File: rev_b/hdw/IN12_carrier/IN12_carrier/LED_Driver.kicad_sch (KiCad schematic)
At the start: 20 parts, among them U2101 LP5009

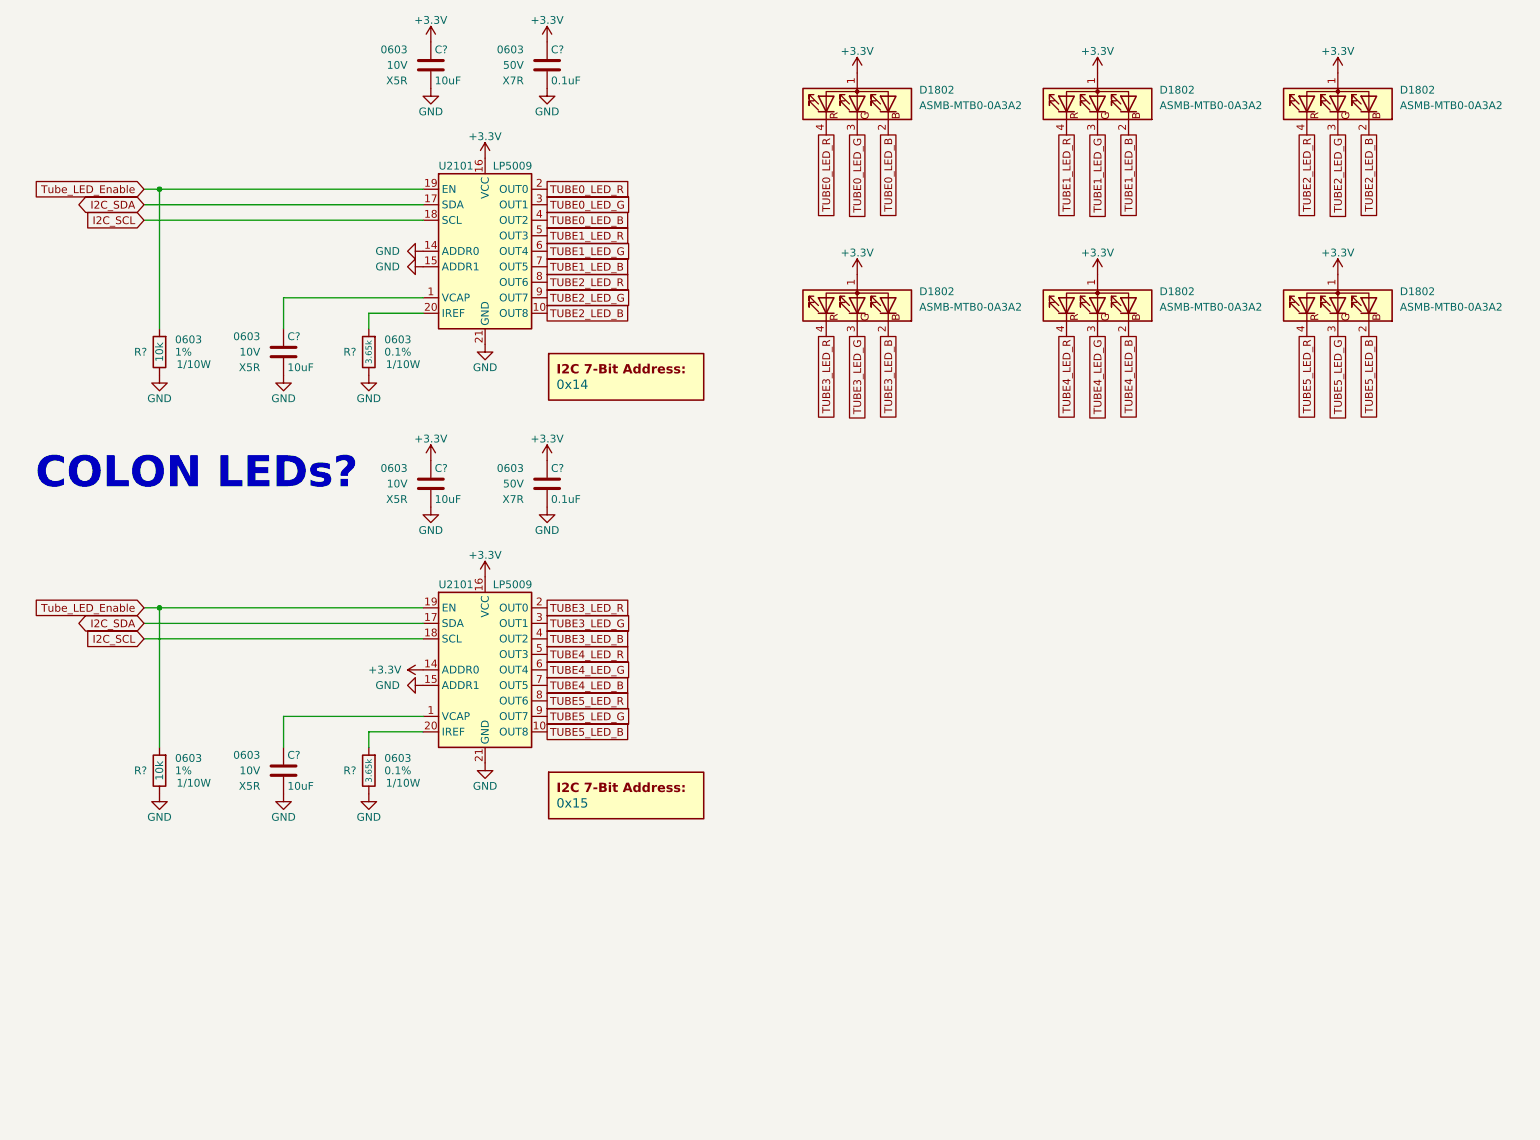
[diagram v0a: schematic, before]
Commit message: updated footprints, ran some DRC
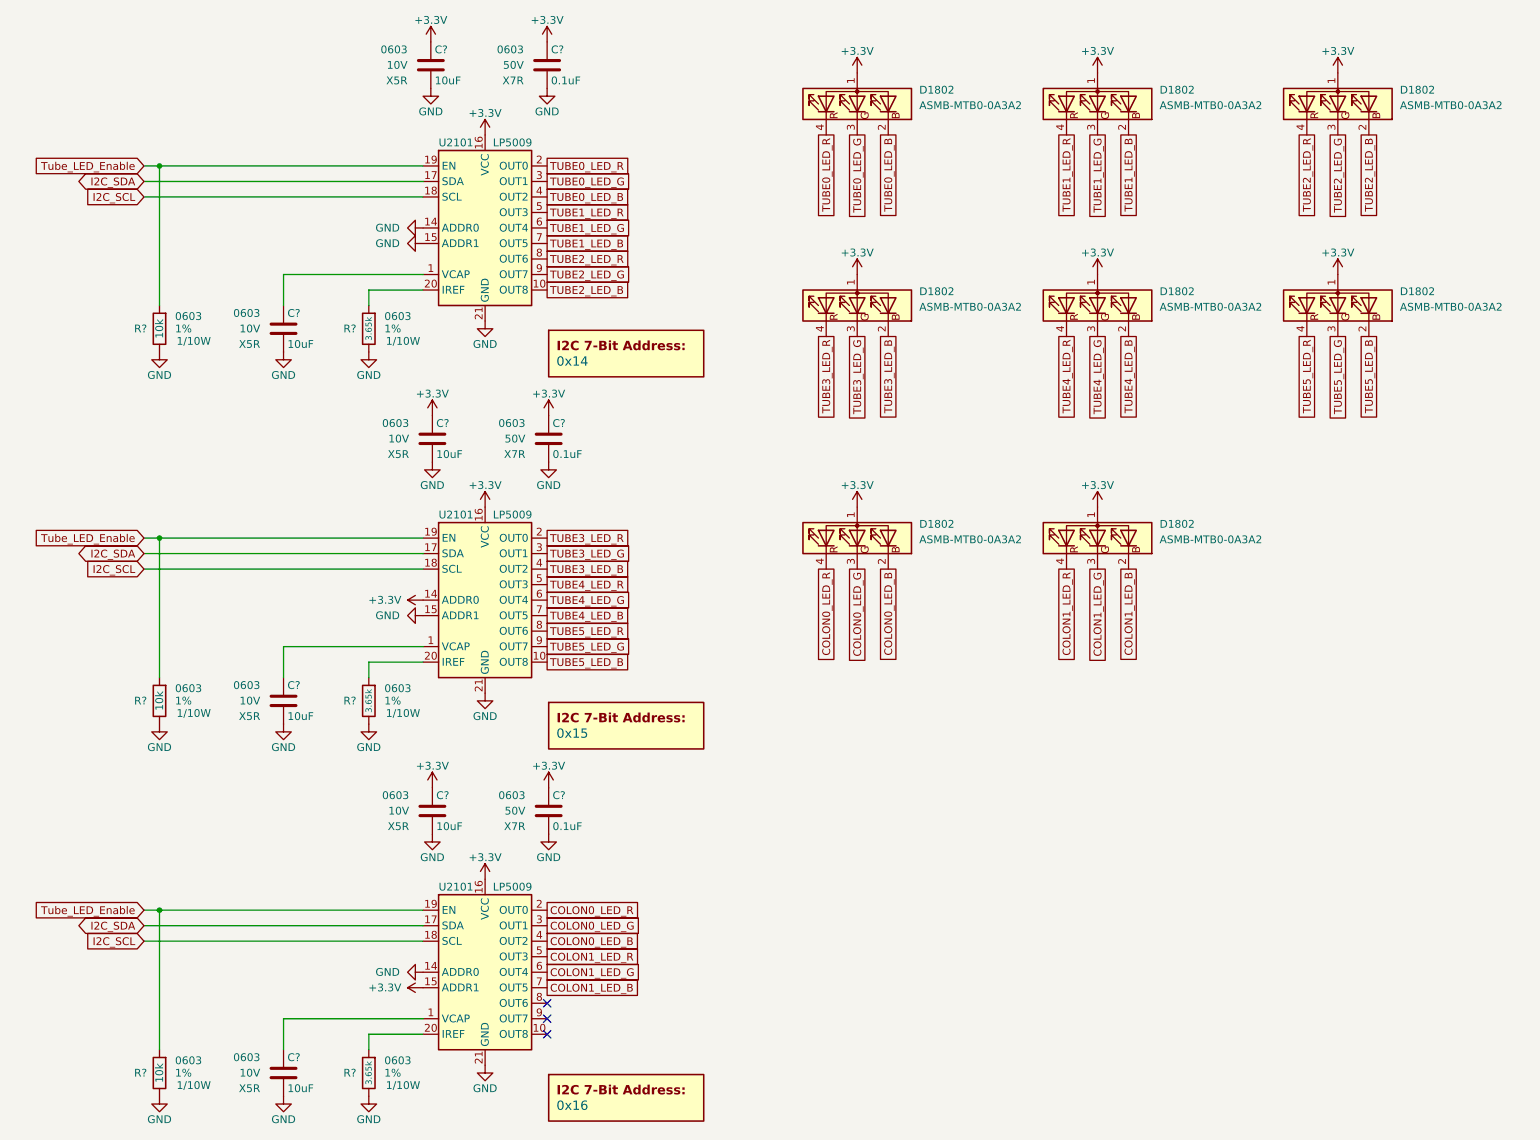
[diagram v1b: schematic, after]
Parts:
- added C?: 0.1uF, Capacitors_SMD:C_0603, symbol Custom_Library:C_Custom
- added C? (x2): 10uF, Capacitors_SMD:C_0603, symbol Custom_Library:C_Custom
- added D1802 (x2): ASMB-MTB0-0A3A2, LED_SMD:LED_Avago_PLCC4_3.2x2.8mm_CW, symbol LED:ASMB-MTB0-0A3A2
- added DOC2101: 0x16, symbol Custom_Library:I2C_Address
- added R?: 10k, Resistors_SMD:R_0603, symbol Custom_Library:R_Custom
- added R?: 3.65k, Resistors_SMD:R_0603, symbol Custom_Library:R_Custom
- added U2101: LP5009, Housings_DFN_QFN:UQFN-20-1EP_3x3mm_Pitch0.4mm, symbol Custom_Library:LP5009
- C? (x2): Digi-Key PN 399-7845-1-ND -> (none)
- C? (x4): Digi-Key PN 490-10474-1-ND -> (none)
- R? (x2): Digi-Key PN YAG2321CT-ND -> (none)
- R? (x2): Digi-Key PN YAG4547CT-ND -> (none); Tolerance 0.1% -> 1%
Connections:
- net +3V3: now also C?.1, C?.1, D1802.1 (A), D1802.1 (A), U2101.15 (ADDR1), U2101.16 (VCC)
- net GND: now also C?.2, C?.2, C?.2, R?.2, R?.2, U2101.14 (ADDR0), U2101.21 (GND)
- net I2C_SCL: now also U2101.18 (SCL)
- net I2C_SDA: now also U2101.17 (SDA)
- net Tube_LED_Enable: now also R?.1, U2101.19 (EN)
- new net: R?.1, U2101.20 (IREF)
- new net: C?.1, U2101.1 (VCAP)
- new net COLON0_LED_B: D1802.2 (BK), U2101.4 (OUT2)
- new net COLON0_LED_G: D1802.3 (GK), U2101.3 (OUT1)
- new net COLON0_LED_R: D1802.4 (RK), U2101.2 (OUT0)
- new net COLON1_LED_B: D1802.2 (BK), U2101.7 (OUT5)
- new net COLON1_LED_G: D1802.3 (GK), U2101.6 (OUT4)
- new net COLON1_LED_R: D1802.4 (RK), U2101.5 (OUT3)
- no-connect marks 0 -> 3
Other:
- note removed: "COLON LEDs?"
- moved on the sheet: C?, R?, U2101

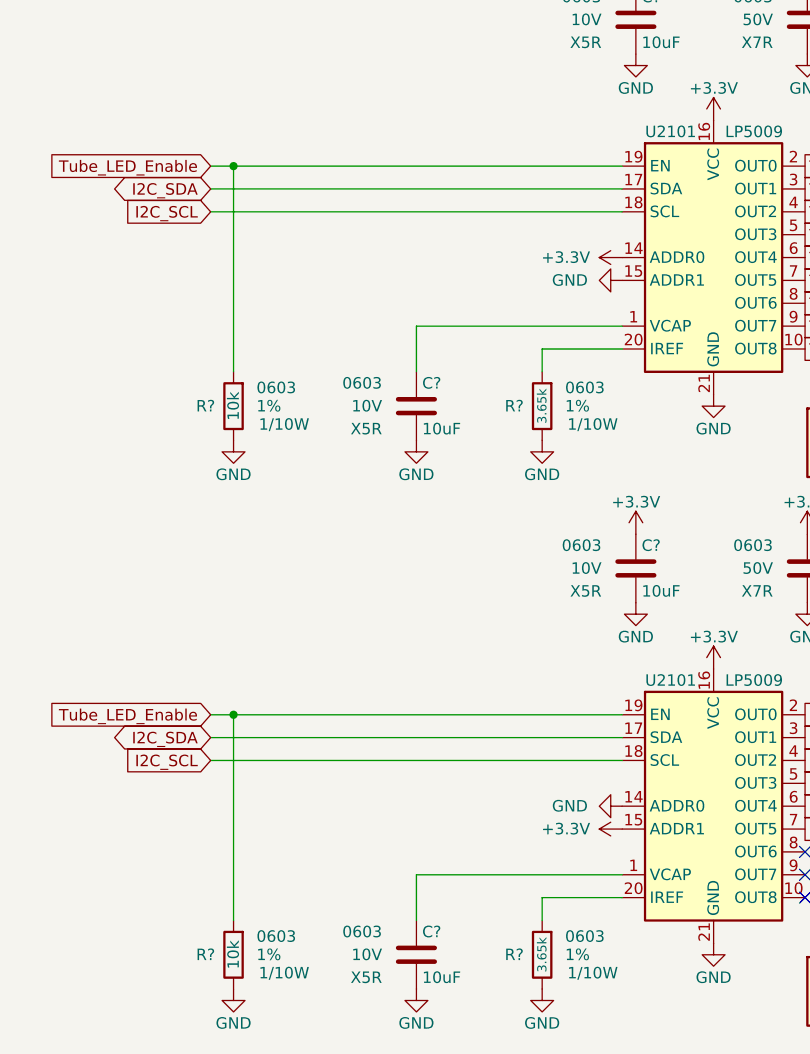
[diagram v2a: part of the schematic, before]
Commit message: lots of placement progress on IN12 carrier board
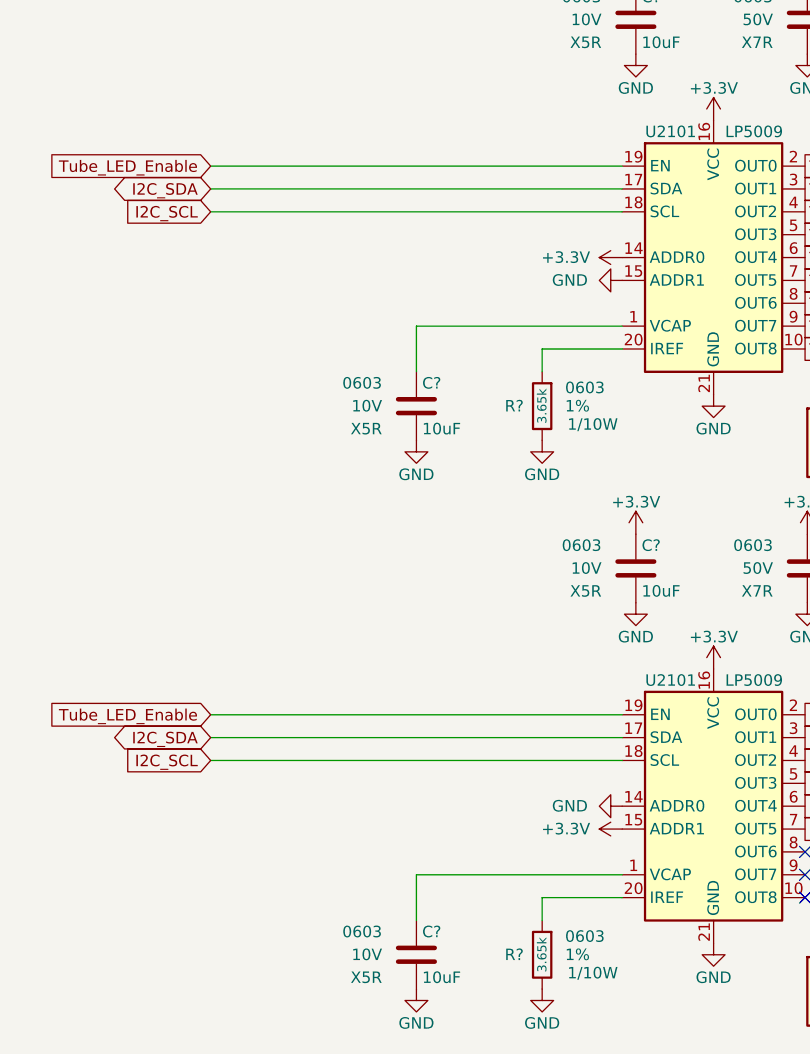
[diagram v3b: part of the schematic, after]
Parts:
- removed R? (x2): 10k, Resistors_SMD:R_0603, symbol Custom_Library:R_Custom
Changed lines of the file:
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@@
     (company "Drew Maatman")
-  )
-  (junction (at 40.64 105.41) (diameter 0) (color 0 0 0 0)
-  )
-  (junction (at 40.64 166.37) (diameter 0) (color 0 0 0 0)
   )
   (junction (at 40.64 44.45) (diameter 0) (color 0 0 0 0)
@@
     (stroke (width 0) (type default))
   )
-  (wire (pts (xy 40.64 105.41) (xy 83.82 105.41))
+  (wire (pts (xy 38.1 105.41) (xy 83.82 105.41))
     (stroke (width 0) (type default))
   )
-  (wire (pts (xy 40.64 166.37) (xy 83.82 166.37))
+  (wire (pts (xy 38.1 166.37) (xy 83.82 166.37))
     (stroke (width 0) (type default))
   )
@@
     (stroke (width 0) (type default))
   )
-  (wire (pts (xy 40.64 189.23) (xy 40.64 166.37))
-    (stroke (width 0) (type default))
-  )
   (wire (pts (xy 60.96 62.23) (xy 60.96 67.31))
     (stroke (width 0) (type default))
@@
     (stroke (width 0) (type default))
   )
-  (wire (pts (xy 38.1 166.37) (xy 40.64 166.37))
-    (stroke (width 0) (type default))
-  )
   (wire (pts (xy 83.82 123.19) (xy 60.96 123.19))
     (stroke (width 0) (type default))
   )
   (wire (pts (xy 38.1 171.45) (xy 83.82 171.45))
-    (stroke (width 0) (type default))
-  )
-  (wire (pts (xy 38.1 105.41) (xy 40.64 105.41))
-    (stroke (width 0) (type default))
-  )
-  (wire (pts (xy 40.64 128.27) (xy 40.64 105.41))
     (stroke (width 0) (type default))
   )
@@
     )
   )
-  (symbol (lib_id "Custom_Library:R_Custom") (at 40.64 193.04 0) (unit 1)
-    (in_bom yes) (on_board yes) (dnp no)
-    (property "Reference" "R?" (at 38.608 193.04 0)
-      (effects (font (size 1.27 1.27)) (justify right))
-    )
-    (property "Value" "10k" (at 40.64 193.04 90)
-      (effects (font (size 1.27 1.27)))
-    )
-    (property "Footprint" "Resistors_SMD:R_0603" (at 40.64 193.04 0)
-      (effects (font (size 1.27 1.27)) hide)
-    )
-    (property "Datasheet" "" (at 40.64 193.04 0)
-      (effects (font (size 1.27 1.27)) hide)
-    )
-    (property "display_footprint" "0603" (at 43.18 191.008 0)
-      (effects (font (size 1.27 1.27)) (justify left))
-    )
-    (property "Tolerance" "1%" (at 43.18 193.04 0)
-      (effects (font (size 1.27 1.27)) (justify left))
-    )
-    (property "Wattage" "1/10W" (at 43.434 195.072 0)
-      (effects (font (size 1.27 1.27)) (justify left))
-    )
-    (property "Digi-Key PN" "" (at 48.26 182.88 0)
-      (effects (font (size 1.524 1.524)) hide)
-    )
-    (pin "1")
-    (pin "2")
-    (instances
-      (project "Analog_Clock"
-        (path "/b40d07ca-3b69-4fcb-b15e-f8aade07e509/00000000-0000-0000-0000-00005bb27bf7"
-          (reference "R?") (unit 1)
-        )
-        (path "/b40d07ca-3b69-4fcb-b15e-f8aade07e509/00000000-0000-0000-0000-00005c1e3a08"
-          (reference "R?") (unit 1)
-        )
-        (path "/b40d07ca-3b69-4fcb-b15e-f8aade07e509/00000000-0000-0000-0000-00005cb7718d"
-          (reference "R?") (unit 1)
-        )
-        (path "/b40d07ca-3b69-4fcb-b15e-f8aade07e509/00000000-0000-0000-0000-00005e0f263a"
-          (reference "R?") (unit 1)
-        )
-        (path "/b40d07ca-3b69-4fcb-b15e-f8aade07e509/00000000-0000-0000-0000-00005e98cf45"
-          (reference "R?") (unit 1)
-        )
-        (path "/b40d07ca-3b69-4fcb-b15e-f8aade07e509/00000000-0000-0000-0000-00005bb27ba3"
-          (reference "R?") (unit 1)
-        )
-        (path "/b40d07ca-3b69-4fcb-b15e-f8aade07e509/00000000-0000-0000-0000-00005d779ae1"
-          (reference "R?") (unit 1)
-        )
-        (path "/b40d07ca-3b69-4fcb-b15e-f8aade07e509/00000000-0000-0000-0000-00005e939d31"
-          (reference "R?") (unit 1)
-        )
-        (path "/b40d07ca-3b69-4fcb-b15e-f8aade07e509/00000000-0000-0000-0000-00005c1de17a"
-          (reference "R?") (unit 1)
-        )
-        (path "/b40d07ca-3b69-4fcb-b15e-f8aade07e509/00000000-0000-0000-0000-00005f280e04"
-          (reference "R2101") (unit 1)
-        )
-        (path "/b40d07ca-3b69-4fcb-b15e-f8aade07e509/00000000-0000-0000-0000-00005e0dc082"
-          (reference "R?") (unit 1)
-        )
-      )
-      (project "IN12_carrier"
-        (path "/c4d83a5b-e6ae-4326-9df5-0c4ac01f7d8c/c710c274-9ef6-4493-9995-cccebf092ebf"
-          (reference "R703") (unit 1)
-        )
-      )
-    )
-  )
   (symbol (lib_id "Analog_Clock-rescue:+3.3V-power") (at 85.344 146.304 0) (unit 1)
     (in_bom yes) (on_board yes) (dnp no)
@@
         (path "/c4d83a5b-e6ae-4326-9df5-0c4ac01f7d8c/c710c274-9ef6-4493-9995-cccebf092ebf"
           (reference "#PWR0734") (unit 1)
-        )
-      )
-    )
-  )
-  (symbol (lib_id "Custom_Library:R_Custom") (at 40.64 132.08 0) (unit 1)
-    (in_bom yes) (on_board yes) (dnp no)
-    (property "Reference" "R?" (at 38.608 132.08 0)
-      (effects (font (size 1.27 1.27)) (justify right))
-    )
-    (property "Value" "10k" (at 40.64 132.08 90)
-      (effects (font (size 1.27 1.27)))
-    )
-    (property "Footprint" "Resistors_SMD:R_0603" (at 40.64 132.08 0)
-      (effects (font (size 1.27 1.27)) hide)
-    )
-    (property "Datasheet" "" (at 40.64 132.08 0)
-      (effects (font (size 1.27 1.27)) hide)
-    )
-    (property "display_footprint" "0603" (at 43.18 130.048 0)
-      (effects (font (size 1.27 1.27)) (justify left))
-    )
-    (property "Tolerance" "1%" (at 43.18 132.08 0)
-      (effects (font (size 1.27 1.27)) (justify left))
-    )
-    (property "Wattage" "1/10W" (at 43.434 134.112 0)
-      (effects (font (size 1.27 1.27)) (justify left))
-    )
-    (property "Digi-Key PN" "" (at 48.26 121.92 0)
-      (effects (font (size 1.524 1.524)) hide)
-    )
-    (pin "1")
-    (pin "2")
-    (instances
-      (project "Analog_Clock"
-        (path "/b40d07ca-3b69-4fcb-b15e-f8aade07e509/00000000-0000-0000-0000-00005bb27bf7"
-          (reference "R?") (unit 1)
-        )
-        (path "/b40d07ca-3b69-4fcb-b15e-f8aade07e509/00000000-0000-0000-0000-00005c1e3a08"
-          (reference "R?") (unit 1)
-        )
-        (path "/b40d07ca-3b69-4fcb-b15e-f8aade07e509/00000000-0000-0000-0000-00005cb7718d"
-          (reference "R?") (unit 1)
-        )
-        (path "/b40d07ca-3b69-4fcb-b15e-f8aade07e509/00000000-0000-0000-0000-00005e0f263a"
-          (reference "R?") (unit 1)
-        )
-        (path "/b40d07ca-3b69-4fcb-b15e-f8aade07e509/00000000-0000-0000-0000-00005e98cf45"
-          (reference "R?") (unit 1)
-        )
-        (path "/b40d07ca-3b69-4fcb-b15e-f8aade07e509/00000000-0000-0000-0000-00005bb27ba3"
-          (reference "R?") (unit 1)
-        )
-        (path "/b40d07ca-3b69-4fcb-b15e-f8aade07e509/00000000-0000-0000-0000-00005d779ae1"
-          (reference "R?") (unit 1)
-        )
-        (path "/b40d07ca-3b69-4fcb-b15e-f8aade07e509/00000000-0000-0000-0000-00005e939d31"
-          (reference "R?") (unit 1)
-        )
-        (path "/b40d07ca-3b69-4fcb-b15e-f8aade07e509/00000000-0000-0000-0000-00005c1de17a"
-          (reference "R?") (unit 1)
-        )
-        (path "/b40d07ca-3b69-4fcb-b15e-f8aade07e509/00000000-0000-0000-0000-00005f280e04"
-          (reference "R2101") (unit 1)
-        )
-        (path "/b40d07ca-3b69-4fcb-b15e-f8aade07e509/00000000-0000-0000-0000-00005e0dc082"
-          (reference "R?") (unit 1)
-        )
-      )
-      (project "IN12_carrier"
-        (path "/c4d83a5b-e6ae-4326-9df5-0c4ac01f7d8c/c710c274-9ef6-4493-9995-cccebf092ebf"
-          (reference "R702") (unit 1)
         )
       )
@@
         (path "/c4d83a5b-e6ae-4326-9df5-0c4ac01f7d8c/c710c274-9ef6-4493-9995-cccebf092ebf"
           (reference "#PWR0738") (unit 1)
-        )
-      )
-    )
-  )
-  (symbol (lib_id "power:GND") (at 40.64 135.89 0) (unit 1)
-    (in_bom yes) (on_board yes) (dnp no)
-    (property "Reference" "#PWR02101" (at 40.64 142.24 0)
-      (effects (font (size 1.27 1.27)) hide)
-    )
-    (property "Value" "GND" (at 40.64 139.7 0)
-      (effects (font (size 1.27 1.27)))
-    )
-    (property "Footprint" "" (at 40.64 135.89 0)
-      (effects (font (size 1.27 1.27)) hide)
-    )
-    (property "Datasheet" "" (at 40.64 135.89 0)
-      (effects (font (size 1.27 1.27)) hide)
-    )
-    (pin "1")
-    (instances
-      (project "Analog_Clock"
-        (path "/b40d07ca-3b69-4fcb-b15e-f8aade07e509/00000000-0000-0000-0000-00005f280e04"
-          (reference "#PWR02101") (unit 1)
-        )
-        (path "/b40d07ca-3b69-4fcb-b15e-f8aade07e509/00000000-0000-0000-0000-00005e98cf45"
-          (reference "#PWR?") (unit 1)
-        )
-      )
-      (project "IN12_carrier"
-        (path "/c4d83a5b-e6ae-4326-9df5-0c4ac01f7d8c/c710c274-9ef6-4493-9995-cccebf092ebf"
-          (reference "#PWR0712") (unit 1)
         )
       )
@@
         )
       )
-    )
-  )
-  (symbol (lib_id "power:GND") (at 40.64 196.85 0) (unit 1)
-    (in_bom yes) (on_board yes) (dnp no)
-    (property "Reference" "#PWR02101" (at 40.64 203.2 0)
-      (effects (font (size 1.27 1.27)) hide)
-    )
-    (property "Value" "GND" (at 40.64 200.66 0)
-      (effects (font (size 1.27 1.27)))
-    )
-    (property "Footprint" "" (at 40.64 196.85 0)
-      (effects (font (size 1.27 1.27)) hide)
-    )
-    (property "Datasheet" "" (at 40.64 196.85 0)
-      (effects (font (size 1.27 1.27)) hide)
-    )
-    (pin "1")
-    (instances
-      (project "Analog_Clock"
-        (path "/b40d07ca-3b69-4fcb-b15e-f8aade07e509/00000000-0000-0000-0000-00005f280e04"
-          (reference "#PWR02101") (unit 1)
-        )
-        (path "/b40d07ca-3b69-4fcb-b15e-f8aade07e509/00000000-0000-0000-0000-00005e98cf45"
-          (reference "#PWR?") (unit 1)
-        )
-      )
-      (project "IN12_carrier"
-        (path "/c4d83a5b-e6ae-4326-9df5-0c4ac01f7d8c/c710c274-9ef6-4493-9995-cccebf092ebf"
-          (reference "#PWR0729") (unit 1)
-        )
-      )
